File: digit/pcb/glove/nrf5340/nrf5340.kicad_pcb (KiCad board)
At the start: 2 copper layers, 91.3 x 54.9 mm, 73 parts, among them IC1 DRV2605LDGSR, IC2 DRV2605LDGSR, IC3 LTC3119EFE#PBF, IC4 TCA9546ADR, J1 Conn_01x02_Pin, J10 USB_C_Receptacle_USB2.0_16P, J11 Conn_01x05_Pin, J12 Conn_01x02_Pin, J13 Conn_01x02_Pin, J14 Conn_01x02_Pin, J15 Conn_01x02_Pin, J17 Conn_01x02_Pin, J18 Conn_01x04_Pin, J2 Conn_01x02_Pin, J3 Conn_01x02_Pin, J4 Conn_01x03_Pin, J5 Conn_01x02_Pin, J6 Conn_01x02_Pin, J7 Conn_01x01_Pin, J8 Conn_01x02_Pin, J9 Conn_01x02_Pin, SW1 SW_Push, U1 ESP32-S3-WROOM-1

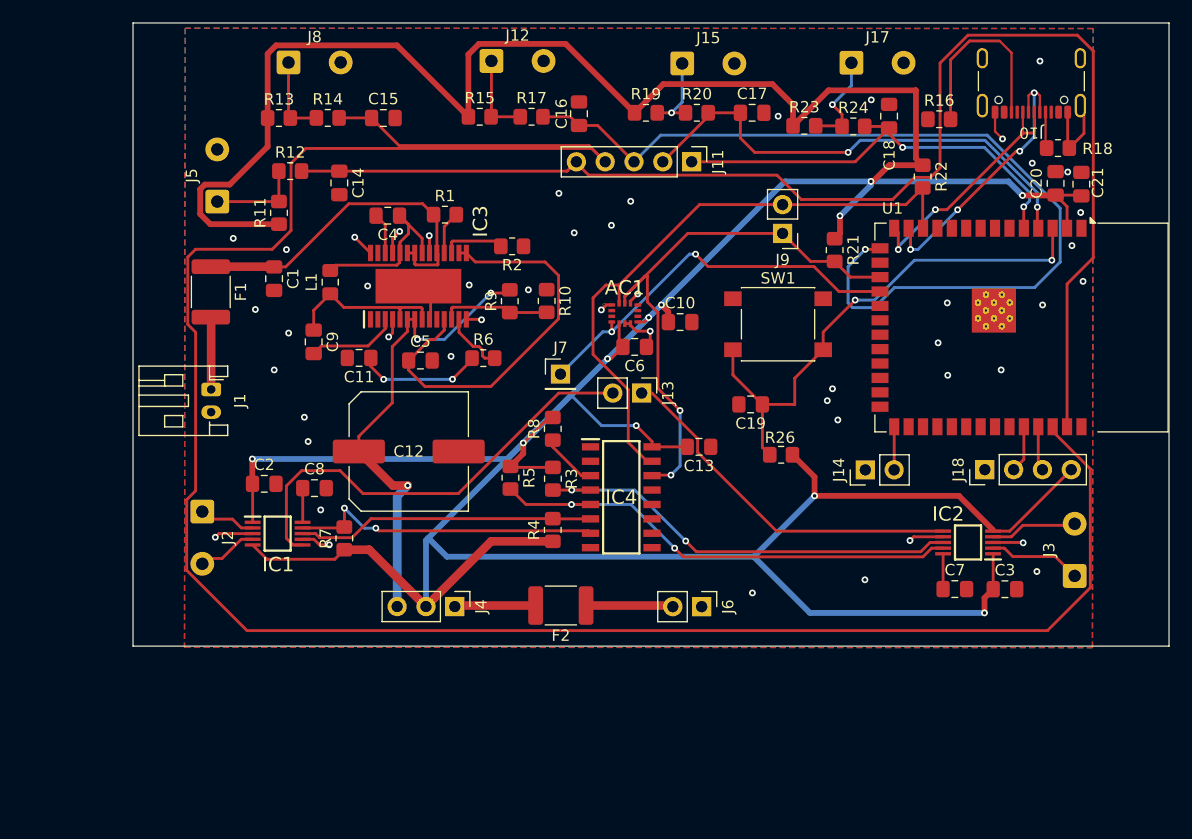
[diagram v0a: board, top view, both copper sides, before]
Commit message: Changed directory names to be proper
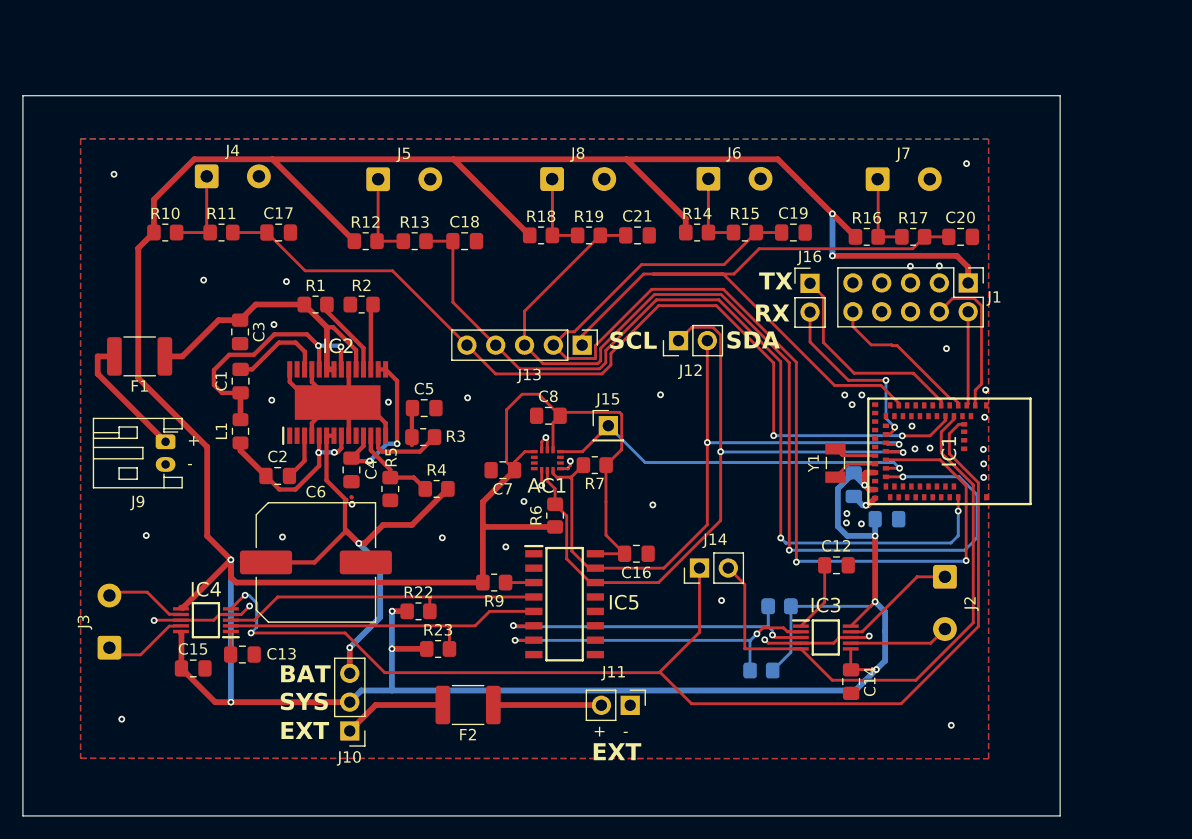
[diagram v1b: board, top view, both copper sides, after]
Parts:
- removed C11: 470pF, Capacitor_SMD:C_0805_2012Metric_Pad1.18x1.45mm_HandSolder
- removed J17: Conn_01x02_Pin, Connector_Wire:SolderWire-0.5sqmm_1x02_P4.6mm_D0.9mm_OD2.1mm
- removed J18: Conn_01x04_Pin, Connector_PinHeader_2.54mm:PinHeader_1x04_P2.54mm_Vertical
- removed R24: 1k, Resistor_SMD:R_0805_2012Metric_Pad1.20x1.40mm_HandSolder
- removed R26, R8: 10k, Resistor_SMD:R_0805_2012Metric_Pad1.20x1.40mm_HandSolder
- removed SW1: SW_Push, Button_Switch_SMD:SW_SPST_PTS645
- removed U1: ESP32-S3-WROOM-1, RF_Module:ESP32-S3-WROOM-1
- added IC5: TCA9546ADR, TCA9546ADR:SOIC127P600X175-16N, F.Cu at (139.2, 113.4)
- added J16: Conn_01x02_Pin, Connector_PinHeader_2.54mm:PinHeader_1x02_P2.54mm_Vertical, F.Cu at (160.8, 85.1)
- added Y1: FC-135R_32.7680KA-AG0, FC-135R_32.768KA-AGO:XTAL_FC-135R_32.7680KA-AG0, F.Cu at (163.1, 101.0)
- C1: value 10µF -> 0.1µF
- C10: value 100nF -> 4.7µF; moved to B.Cu
- C12: value 150µF -> 1µF; footprint Capacitor_SMD:C_Elec_10x10.2 -> Capacitor_SMD:C_0805_2012Metric_Pad1.18x1.45mm_HandSolder
- C13: value 0.1µF -> 1µF
- C14, C15: value 100nF -> 1µF
- C16: value 100nF -> 0.1µF
- C19, C20: value 0.1uF -> 100nF
- C2: value 1µF -> 0.1µF
- C21: value 22uF -> 100nF
- C3: value 1µF -> 10µF
- C4: value 0.1µF -> 4.7µF
- C5: value 4.7µF -> 470pF
- C6: value 100nF -> 150µF; footprint Capacitor_SMD:C_0805_2012Metric_Pad1.18x1.45mm_HandSolder -> Capacitor_SMD:C_Elec_10x10.2
- C7, C8: value 1µF -> 100nF
- C9: value 0.1µF -> 2.2µF; moved to B.Cu
- IC1: value DRV2605LDGSR -> MDBT53-P1M; footprint DRV2605LDGSR:SOP50P490X110-10N -> MDBT53-P1M:MDBT53P1M
- IC2: value DRV2605LDGSR -> LTC3119EFE#PBF; footprint DRV2605LDGSR:SOP50P490X110-10N -> LTC3119EFE#PBF:SOP65P640X120-29N
- IC3: value LTC3119EFE#PBF -> DRV2605LDGSR; footprint LTC3119EFE#PBF:SOP65P640X120-29N -> DRV2605LDGSR:SOP50P490X110-10N
- IC4: value TCA9546ADR -> DRV2605LDGSR; footprint TCA9546ADR:SOIC127P600X175-16N -> DRV2605LDGSR:SOP50P490X110-10N
- J1: value Conn_01x02_Pin -> Conn_02x05_Odd_Even; footprint Connector_JST:JST_PH_S2B-PH-K_1x02_P2.00mm_Horizontal -> Connector_PinHeader_2.54mm:PinHeader_2x05_P2.54mm_Vertical
- J10: value USB_C_Receptacle_USB2.0_16P -> Conn_01x03_Pin; footprint Connector_USB:USB_C_Receptacle_GCT_USB4105-xx-A_16P_TopMnt_Horizontal -> Connector_PinHeader_2.54mm:PinHeader_1x03_P2.54mm_Vertical
- J11: value Conn_01x05_Pin -> Conn_01x02_Pin; footprint Connector_PinHeader_2.54mm:PinHeader_1x05_P2.54mm_Vertical -> Connector_PinHeader_2.54mm:PinHeader_1x02_P2.54mm_Vertical
- J12: footprint Connector_Wire:SolderWire-0.5sqmm_1x02_P4.6mm_D0.9mm_OD2.1mm -> Connector_PinHeader_2.54mm:PinHeader_1x02_P2.54mm_Vertical
- J13: value Conn_01x02_Pin -> Conn_01x05_Pin; footprint Connector_PinHeader_2.54mm:PinHeader_1x02_P2.54mm_Vertical -> Connector_PinHeader_2.54mm:PinHeader_1x05_P2.54mm_Vertical
- J15: value Conn_01x02_Pin -> Conn_01x01_Pin; footprint Connector_Wire:SolderWire-0.5sqmm_1x02_P4.6mm_D0.9mm_OD2.1mm -> Connector_PinHeader_2.54mm:PinHeader_1x01_P2.54mm_Vertical
- J4: value Conn_01x03_Pin -> Conn_01x02_Pin; footprint Connector_PinHeader_2.54mm:PinHeader_1x03_P2.54mm_Vertical -> Connector_Wire:SolderWire-0.5sqmm_1x02_P4.6mm_D0.9mm_OD2.1mm
- J6: footprint Connector_PinHeader_2.54mm:PinHeader_1x02_P2.54mm_Vertical -> Connector_Wire:SolderWire-0.5sqmm_1x02_P4.6mm_D0.9mm_OD2.1mm
- J7: value Conn_01x01_Pin -> Conn_01x02_Pin; footprint Connector_PinHeader_2.54mm:PinHeader_1x01_P2.54mm_Vertical -> Connector_Wire:SolderWire-0.5sqmm_1x02_P4.6mm_D0.9mm_OD2.1mm
- J9: footprint Connector_PinHeader_2.54mm:PinHeader_1x02_P2.54mm_Vertical -> Connector_JST:JST_PH_S2B-PH-K_1x02_P2.00mm_Horizontal
- R10: value 100k -> 22k
- R11, R13, R15, R19: value 22k -> 1k
- R12, R14: value 1k -> 22k
- R16, R18: value 5.1k -> 22k
- R20: value 1k -> 10k; moved to B.Cu
- R21: moved to B.Cu
- R23: value 22k -> 10k
- R3: value 10k -> 52.3k
- R4: value 10k -> 316k
- R5: value 10k -> 100k
- R6: value 52.3k -> 10k
- R9: value 316k -> 10k
- moved J3 85.3 mm to (99.1, 117.2)
- moved J10 83.7 mm to (120.3, 124.6)
- moved C3 71.1 mm to (110.6, 89.4), turned to -90 degrees
- moved J1 67.4 mm to (174.8, 85.1)
- moved J2 65.7 mm to (172.7, 111.0)
- moved C14 63.0 mm to (164.4, 120.2)
- moved IC1 59.7 mm to (173.1, 99.9), turned to -90 degrees
- moved R22 58.7 mm to (126.3, 114.0), turned to 0 degrees
- moved J9 57.4 mm to (104.0, 99.1), turned to -90 degrees
- moved IC2 56.9 mm to (119.2, 95.6), turned to 90 degrees
- moved R23 56.3 mm to (128.0, 117.4)
- moved C15 51.3 mm to (106.5, 119.1)
- moved R20 49.5 mm to (156.5, 119.3), turned to 180 degrees
- moved C9 49.3 mm to (164.7, 102.9)
- moved J11 48.2 mm to (145.0, 122.3)
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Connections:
- C1 pad 1: Net-(IC3-PVIN_1) -> Net-(IC2-SW1_1)
- C1 pad 2: GND -> Net-(IC2-BST1)
- C12 pad 1: /BB_3V3 -> Net-(IC3-REG)
- C13 pad 1: GND -> Net-(IC4-REG)
- C13 pad 2: SYS_3V3 -> GND
- C14 pad 1: /FLEX1_ADC -> SYS_3V3
- C15 pad 1: /FLEX2_ADC -> SYS_3V3
- C16 pad 1: /FLEX3_ADC -> GND
- C16 pad 2: GND -> SYS_3V3
- C17 pad 1: /FLEX4_ADC -> /FLEX1_ADC
- C18 pad 1: /FLEX5_ADC -> /FLEX2_ADC
- C19 pad 1: /EN -> /FLEX4_ADC
- C2 pad 1: SYS_3V3 -> Net-(IC2-SW2_1)
- C2 pad 2: GND -> Net-(IC2-BST2)
- C20 pad 1: SYS_3V3 -> /FLEX5_ADC
- C21 pad 1: SYS_3V3 -> /FLEX3_ADC
- C3 pad 1: SYS_3V3 -> Net-(IC2-PVIN_1)
- C4 pad 1: Net-(IC3-SW1_1) -> Net-(IC2-MPPC)
- C4 pad 2: Net-(IC3-BST1) -> GND
- C5 pad 1: Net-(IC3-MPPC) -> Net-(C5-Pad1)
- C6 pad 1: GND -> /BB_3V3
- C6 pad 2: SYS_3V3 -> GND
- C7 pad 1: Net-(IC2-VDD) -> SYS_3V3
- C8 pad 1: Net-(IC1-VDD) -> GND
- C8 pad 2: GND -> SYS_3V3
- C9 pad 1: Net-(IC3-SW2_1) -> SYS_3V3
- C9 pad 2: Net-(IC3-BST2) -> GND
- F1 pad 1: Net-(IC3-PVIN_1) -> Net-(IC2-PVIN_1)
- F2 pad 2: Net-(J4-Pin_1) -> Net-(J10-Pin_1)
- IC1 pad 1: SYS_3V3 -> GND
- IC1 pad 10: Net-(IC1-VDD) -> /UART_TX
- IC1 pad 2: Net-(IC1-SCL) -> /SWDCLK
- IC1 pad 3: GND -> unconnected-(IC1-P1.08-Pad3)
- IC1 pad 4: Net-(IC1-IN/TRIG) -> /SWDIO
- IC1 pad 5: SYS_3V3 -> unconnected-(IC1-P0.27-Pad5)
- IC1 pad 6: /HAPTIC_DRIVER1_EN -> /RESET
- IC1 pad 7: GND -> /HAPTIC_DRIVER1_EN
- IC1 pad 8: Net-(IC1-GND) -> unconnected-(IC1-P0.24-Pad8)
- IC1 pad 9: Net-(IC1-OUT-) -> /FLEX1_ADC
- IC2 pad 1: SYS_3V3 -> unconnected-(IC2-N/C_1-Pad1)
- IC2 pad 10: Net-(IC2-VDD) -> unconnected-(IC2-PGOOD-Pad10)
- IC2 pad 2: Net-(IC2-SCL) -> unconnected-(IC2-N/C_2-Pad2)
- IC2 pad 3: GND -> Net-(IC2-BST2)
- IC2 pad 4: Net-(IC2-IN/TRIG) -> GND
- IC2 pad 5: SYS_3V3 -> Net-(IC2-SW2_1)
- IC2 pad 6: /HAPTIC_DRIVER2_EN -> /BB_3V3
- IC2 pad 7: GND -> /BB_3V3
- IC2 pad 8: Net-(IC2-GND) -> Net-(IC2-SW2_1)
- IC2 pad 9: Net-(IC2-OUT-) -> GND
- IC3 pad 1: unconnected-(IC3-N/C_1-Pad1) -> Net-(IC3-REG)
- IC3 pad 10: unconnected-(IC3-PGOOD-Pad10) -> SYS_3V3
- IC3 pad 2: unconnected-(IC3-N/C_2-Pad2) -> Net-(IC3-SCL)
- IC3 pad 3: Net-(IC3-BST2) -> Net-(IC3-SDA)
- IC3 pad 5: Net-(IC3-SW2_1) -> /HAPTIC_DRIVER1_EN
- IC3 pad 6: /BB_3V3 -> SYS_3V3
- IC3 pad 7: /BB_3V3 -> Net-(IC3-OUT+)
- IC3 pad 8: Net-(IC3-SW2_1) -> GND
- IC3 pad 9: GND -> Net-(IC3-OUT-)
- IC4 pad 1: GND -> Net-(IC4-REG)
- IC4 pad 10: unconnected-(IC4-SC2-Pad10) -> SYS_3V3
- IC4 pad 2: GND -> Net-(IC4-SCL)
- IC4 pad 3: Net-(IC4-~{RESET}) -> Net-(IC4-SDA)
- IC4 pad 4: Net-(IC2-GND) -> GND
- IC4 pad 5: Net-(IC2-OUT-) -> /HAPTIC_DRIVER2_EN
- IC4 pad 6: Net-(IC1-GND) -> SYS_3V3
- IC4 pad 7: Net-(IC1-OUT-) -> Net-(IC4-OUT+)
- IC4 pad 9: unconnected-(IC4-SD2-Pad9) -> Net-(IC4-OUT-)
- J1 pad 1: +3.7V -> SYS_3V3
- J1 pad 2: GND -> /SWDIO
- J11 pad 1: /FLEX5_ADC -> GND
- J11 pad 2: /FLEX4_ADC -> /EXT_3V3
- J12 pad 1: Net-(J12-Pin_1) -> /I2C_SCL
- J12 pad 2: GND -> /I2C_SDA
- J13 pad 1: /HAPTIC_DRIVER2_EN -> /FLEX5_ADC
- J13 pad 2: /HAPTIC_DRIVER1_EN -> /FLEX4_ADC
- J14 pad 1: GND -> /HAPTIC_DRIVER2_EN
- J14 pad 2: /BOOT -> /HAPTIC_DRIVER1_EN
- J15 pad 1: Net-(J15-Pin_1) -> /IMU_INT1
- J2 pad 1: Net-(IC1-SCL) -> Net-(IC3-OUT-)
- J2 pad 2: Net-(IC1-IN/TRIG) -> Net-(IC3-OUT+)
- J3 pad 1: Net-(IC2-SCL) -> Net-(IC4-OUT-)
- J3 pad 2: Net-(IC2-IN/TRIG) -> Net-(IC4-OUT+)
- J4 pad 2: SYS_3V3 -> GND
- J6 pad 1: GND -> Net-(J6-Pin_1)
- J6 pad 2: /EXT_3V3 -> GND
- J7 pad 1: /IMU_INT1 -> Net-(J7-Pin_1)
- J9 pad 1: /I2C_SCL -> +3.7V
- J9 pad 2: /I2C_SDA -> GND
- L1 pad 1: Net-(IC3-SW2_1) -> Net-(IC2-SW2_1)
- L1 pad 2: Net-(IC3-SW1_1) -> Net-(IC2-SW1_1)
- R1 pad 1: Net-(IC3-PVIN_1) -> Net-(IC2-PVIN_1)
- R1 pad 2: Net-(IC3-RUN) -> Net-(IC2-RUN)
- R10 pad 1: GND -> SYS_3V3
- R10 pad 2: Net-(IC3-FB) -> Net-(J4-Pin_1)
- R11 pad 1: SYS_3V3 -> Net-(J4-Pin_1)
- R11 pad 2: Net-(J5-Pin_1) -> /FLEX1_ADC
- R12 pad 1: Net-(J5-Pin_1) -> SYS_3V3
- R12 pad 2: /FLEX1_ADC -> Net-(J5-Pin_1)
- R13 pad 1: SYS_3V3 -> Net-(J5-Pin_1)
- R13 pad 2: Net-(J8-Pin_1) -> /FLEX2_ADC
- R14 pad 1: Net-(J8-Pin_1) -> SYS_3V3
- R14 pad 2: /FLEX2_ADC -> Net-(J6-Pin_1)
- R15 pad 1: SYS_3V3 -> Net-(J6-Pin_1)
- R15 pad 2: Net-(J12-Pin_1) -> /FLEX4_ADC
- R16 pad 1: GND -> SYS_3V3
- R16 pad 2: Net-(J10-CC2) -> Net-(J7-Pin_1)
- R17 pad 1: Net-(J12-Pin_1) -> Net-(J7-Pin_1)
- R17 pad 2: /FLEX3_ADC -> /FLEX5_ADC
- R18 pad 1: GND -> SYS_3V3
- R18 pad 2: Net-(J10-CC1) -> Net-(J8-Pin_1)
- R19 pad 1: SYS_3V3 -> Net-(J8-Pin_1)
- R19 pad 2: Net-(J15-Pin_1) -> /FLEX3_ADC
- R2 pad 2: Net-(IC3-RT) -> Net-(IC2-RT)
- R20 pad 1: Net-(J15-Pin_1) -> SYS_3V3
- R20 pad 2: /FLEX4_ADC -> Net-(IC3-SCL)
- R21 pad 2: /I2C_SCL -> Net-(IC3-SDA)
- R22 pad 2: /I2C_SDA -> Net-(IC4-SDA)
- R23 pad 2: Net-(J17-Pin_1) -> Net-(IC4-SCL)
- R3 pad 1: SYS_3V3 -> Net-(C5-Pad1)
- R3 pad 2: Net-(IC2-GND) -> Net-(IC2-VC)
- R4 pad 1: SYS_3V3 -> Net-(IC2-FB)
- R4 pad 2: Net-(IC1-GND) -> /BB_3V3
- R5 pad 1: SYS_3V3 -> GND
- R5 pad 2: Net-(IC2-OUT-) -> Net-(IC2-FB)
- R6 pad 1: Net-(C11-Pad1) -> SYS_3V3
- R6 pad 2: Net-(IC3-VC) -> /I2C_SCL
- R7 pad 2: Net-(IC1-OUT-) -> /I2C_SDA
- R9 pad 1: Net-(IC3-FB) -> Net-(IC5-~{RESET})
- R9 pad 2: /BB_3V3 -> SYS_3V3
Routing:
- net /FLEX2_ADC: track 197.0 -> 79.6 mm, vias 0 -> 2
- net /HAPTIC_DRIVER2_EN: track 32.3 -> 105.8 mm, vias 0 -> 2
- net /FLEX4_ADC: track 43.3 -> 99.3 mm
- net /EN: track 46.5 -> 0.00 mm, vias 2 -> 0
- net Net-(IC2-OUT-): track 42.6 -> 0.00 mm, vias 2 -> 0
- net Net-(IC2-GND): track 38.6 -> 0.00 mm, vias 2 -> 0
- net /FLEX1_ADC: track 117.6 -> 80.5 mm, vias 0 -> 2
- net Net-(IC3-MPPC): track 35.8 -> 0.00 mm
- net Net-(IC3-PVIN_1): track 30.6 -> 0.00 mm
- net Net-(IC3-SCL): track 0.00 -> 30.1 mm, vias 0 -> 2
- net Net-(IC3-SDA): track 0.00 -> 29.6 mm, vias 0 -> 2
- net Net-(IC4-SCL): track 0.00 -> 29.3 mm
- net Net-(IC4-SDA): track 0.00 -> 28.9 mm
- net Net-(IC1-OUT-): track 28.0 -> 0.00 mm, vias 2 -> 0
- net Net-(IC2-PVIN_1): track 0.00 -> 26.4 mm
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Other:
- board size 91.3 x 54.9 mm -> 91.4 x 63.5 mm
- board text added: "+"
- board text added: "-"
- board text added: "BAT"
- board text added: "EXT"
- board text added: "RX"
- board text added: "SCL"
- board text added: "SDA"
- board text added: "SYS"
- board text added: "TX"
